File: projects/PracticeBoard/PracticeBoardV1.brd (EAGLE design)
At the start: 160 x 100 mm, 31 parts, among them U1 TPS63001, U3 SNX4AHC08-QUAD-2IN-AND, U4 SN74LV32A-QUAD-2IN-OR

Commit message: PracticeBoardV1 Schematic Review
Added led enable circuit and nonfunctional components
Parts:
- removed R7: (no value), BrownSpaceEngineering:0805
- added C26: 1uF, BrownSpaceEngineering:0805
- added C27, C28: 0.01uF, BrownSpaceEngineering:0805
- added D6: 1N4148SOD-523F, BrownSpaceEngineering:SOD-523F
- added D7: LED0805, BrownSpaceEngineering:0805-D
- added R23: 91K, BrownSpaceEngineering:0805
- added R24, R25: 10K, BrownSpaceEngineering:0805
- added R6: (no value), BrownSpaceEngineering:0805
- added U5: (no value), BrownSpaceEngineering:SO-8
- added U6: SN74LV00A-QUAD-2IN-NAND, BrownSpaceEngineering:TSSOP-14
- added U7: (no value), BrownSpaceEngineering:TSSOP-14
- added U8: SNX4LV86A-QUAD-2IN-XOR, BrownSpaceEngineering:TSSOP-14
- added U9: UA741-OP-AMP, BrownSpaceEngineering:SOIC-8
- added V8: IN4, BrownSpaceEngineering:VIA-60MIL-SQ
- added V9: OUT4, BrownSpaceEngineering:VIA-60MIL-SQ
- R5: device BrownSpaceEngineering:1210 -> BrownSpaceEngineering:0805
- moved R5 241.4 mm to (-4.00, -32.0)
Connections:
- new net !LED_CMD!: C28.1, R25.2, R6.2, V9.P$1
- new net LED_SHDN: D7.A, U5.P$3
- new net N$20: C26.1, R23.2, U5.P$6, U5.P$7
- new net N$23: C27.1, U5.P$5
- new net TRIG: C28.2, D6.A, R24.2, U5.P$2
- net +3V3: now also D6.C, R23.1, R24.1, R25.1, R5.2, U5.P$4, U5.P$8, V8.P$1; no longer R7.2
- net GND: now also C26.2, C27.2, D7.C, R6.1, U5.P$1
- net N$7: now also R5.1; no longer R7.1
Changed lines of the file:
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@@
 <?xml version="1.0" encoding="utf-8"?>
 <!DOCTYPE eagle SYSTEM "eagle.dtd">
-<eagle version="8.3.1">
+<eagle version="8.2.2">
 <drawing>
 <settings>
@@
 <element name="BATTERY" library="BrownSpaceEngineering" package="BC-2003-COIN-BATTERY-HOLDER" value="BC-2003-COIN-BATTERY-HOLDER" x="14" y="-10"/>
 <element name="U2" library="BrownSpaceEngineering" package="SO-8" value="" x="-3" y="-13"/>
-<element name="R7" library="BrownSpaceEngineering" package="0805" value="" x="-4" y="-32"/>
+<element name="R5" library="BrownSpaceEngineering" package="0805" value="" x="-4" y="-32"/>
 <element name="C4" library="BrownSpaceEngineering" package="0805" value="0.01uF" x="-4" y="-42"/>
 <element name="C5" library="BrownSpaceEngineering" package="0805" value="" x="-4" y="-47"/>
@@
 <element name="D4" library="BrownSpaceEngineering" package="0805-D" value="LED0805" x="-12" y="-271"/>
 <element name="D5" library="BrownSpaceEngineering" package="0805-D" value="LED0805" x="-12" y="-276"/>
-<element name="R5" library="BrownSpaceEngineering" package="1210" value="" x="-18" y="-273"/>
+<element name="U5" library="BrownSpaceEngineering" package="SO-8" value="" x="-10" y="-284"/>
+<element name="C26" library="BrownSpaceEngineering" package="0805" value="1uF" x="-12" y="-292"/>
+<element name="C27" library="BrownSpaceEngineering" package="0805" value="0.01uF" x="-8" y="-292"/>
+<element name="C28" library="BrownSpaceEngineering" package="0805" value="0.01uF" x="-4" y="-292"/>
+<element name="R23" library="BrownSpaceEngineering" package="0805" value="91K" x="-12" y="-296"/>
+<element name="R24" library="BrownSpaceEngineering" package="0805" value="10K" x="-8" y="-296"/>
+<element name="R25" library="BrownSpaceEngineering" package="0805" value="10K" x="-4" y="-296"/>
+<element name="D6" library="BrownSpaceEngineering" package="SOD-523F" value="1N4148SOD-523F" x="-5" y="-281"/>
+<element name="V8" library="BrownSpaceEngineering" package="VIA-60MIL-SQ" value="IN4" x="-3" y="-310"/>
+<element name="V9" library="BrownSpaceEngineering" package="VIA-60MIL-SQ" value="OUT4" x="-3" y="-333"/>
+<element name="R6" library="BrownSpaceEngineering" package="0805" value="" x="-12" y="-347"/>
+<element name="D7" library="BrownSpaceEngineering" package="0805-D" value="LED0805" x="-12" y="-352"/>
+<element name="U6" library="BrownSpaceEngineering" package="TSSOP-14" value="SN74LV00A-QUAD-2IN-NAND" x="-18" y="-349"/>
+<element name="U7" library="BrownSpaceEngineering" package="TSSOP-14" value="" x="-26" y="-349"/>
+<element name="U8" library="BrownSpaceEngineering" package="TSSOP-14" value="SNX4LV86A-QUAD-2IN-XOR" x="-34" y="-349"/>
+<element name="U9" library="BrownSpaceEngineering" package="SOIC-8" value="UA741-OP-AMP" x="-41" y="-348"/>
 </elements>
 <signals>
@@
 <vertex x="160" y="0"/>
 </polygon>
-<contactref element="R7" pad="2"/>
+<contactref element="R5" pad="2"/>
 <contactref element="U2" pad="P$8"/>
 <contactref element="U2" pad="P$4"/>
@@
 <contactref element="U3" pad="P14"/>
 <contactref element="U4" pad="P14"/>
+<contactref element="U5" pad="P$8"/>
+<contactref element="U5" pad="P$4"/>
+<contactref element="R24" pad="1"/>
+<contactref element="R25" pad="1"/>
+<contactref element="D6" pad="C"/>
+<contactref element="V8" pad="P$1"/>
+<contactref element="R23" pad="1"/>
 <wire x1="-3" y1="-188" x2="-3" y2="-234" width="0" layer="19" extent="1-1"/>
 <wire x1="-3" y1="-142" x2="-3" y2="-188" width="0" layer="19" extent="1-1"/>
 <wire x1="-4.725" y1="-127.75" x2="-3" y2="-142" width="0" layer="19" extent="1-1"/>
 <wire x1="-11.95" y1="-122.2" x2="-4.725" y2="-127.75" width="0" layer="19" extent="1-1"/>
+<wire x1="-5" y1="-280" x2="-3" y2="-234" width="0" layer="19" extent="1-1"/>
+<wire x1="-11.905" y1="-281.1" x2="-5" y2="-280" width="0" layer="19" extent="1-1"/>
+<wire x1="-8.095" y1="-286.9" x2="-11.905" y2="-281.1" width="0" layer="19" extent="1-1"/>
+<wire x1="-8.9" y1="-296" x2="-8.095" y2="-286.9" width="0" layer="19" extent="1-1"/>
+<wire x1="-12.9" y1="-296" x2="-8.9" y2="-296" width="0" layer="19" extent="1-1"/>
+<wire x1="-4.9" y1="-296" x2="-8.9" y2="-296" width="0" layer="19" extent="1-1"/>
+<wire x1="-3" y1="-310" x2="-4.9" y2="-296" width="0" layer="19" extent="1-1"/>
 <wire x1="-3.1" y1="-32" x2="-11.95" y2="-122.2" width="0" layer="19" extent="1-1"/>
 <wire x1="-1.095" y1="-15.9" x2="-3.1" y2="-32" width="0" layer="19" extent="1-1"/>
@@
 <contactref element="D4" pad="C"/>
 <contactref element="U3" pad="P7"/>
+<contactref element="U5" pad="P$1"/>
+<contactref element="C26" pad="2"/>
+<contactref element="C27" pad="2"/>
+<contactref element="R6" pad="1"/>
+<contactref element="D7" pad="C"/>
 <wire x1="102.49" y1="51.6" x2="106.3" y2="51.6" width="0" layer="19" extent="1-1"/>
 <wire x1="95.21" y1="51.6" x2="102.49" y2="51.6" width="0" layer="19" extent="1-1"/>
@@
 <wire x1="-11.1" y1="-271" x2="-8.05" y2="-127.8" width="0" layer="19" extent="1-1"/>
 <wire x1="-11.1" y1="-276" x2="-11.1" y2="-271" width="0" layer="19" extent="1-1"/>
+<wire x1="-11.905" y1="-286.9" x2="-11.1" y2="-276" width="0" layer="19" extent="1-1"/>
+<wire x1="-11.1" y1="-292" x2="-11.905" y2="-286.9" width="0" layer="19" extent="1-1"/>
+<wire x1="-7.1" y1="-292" x2="-11.1" y2="-292" width="0" layer="19" extent="1-1"/>
+<wire x1="-12.9" y1="-347" x2="-11.1" y2="-292" width="0" layer="19" extent="1-1"/>
+<wire x1="-11.1" y1="-352" x2="-12.9" y2="-347" width="0" layer="19" extent="1-1"/>
 </signal>
 <signal name="3V3REF">
@@
 </signal>
 <signal name="N$7">
-<contactref element="R7" pad="1"/>
+<contactref element="R5" pad="1"/>
 <contactref element="U2" pad="P$7"/>
 <contactref element="POTENTIOMETER-OUT" pad="P$1"/>
@@
 <wire x1="-12.9" y1="-276" x2="-8.7" y2="-127.8" width="0" layer="19" extent="1-1"/>
 </signal>
+<signal name="N$20">
+<contactref element="R23" pad="2"/>
+<contactref element="U5" pad="P$7"/>
+<contactref element="U5" pad="P$6"/>
+<contactref element="C26" pad="1"/>
+<wire x1="-12.9" y1="-292" x2="-11.1" y2="-296" width="0" layer="19" extent="1-1"/>
+<wire x1="-10.635" y1="-281.1" x2="-12.9" y2="-292" width="0" layer="19" extent="1-1"/>
+<wire x1="-9.365" y1="-281.1" x2="-10.635" y2="-281.1" width="0" layer="19" extent="1-1"/>
+</signal>
+<signal name="N$23">
+<contactref element="C27" pad="1"/>
+<contactref element="U5" pad="P$5"/>
+<wire x1="-8.095" y1="-281.1" x2="-8.9" y2="-292" width="0" layer="19" extent="1-1"/>
+</signal>
+<signal name="TRIG">
+<contactref element="C28" pad="2"/>
+<contactref element="U5" pad="P$2"/>
+<contactref element="R24" pad="2"/>
+<contactref element="D6" pad="A"/>
+<wire x1="-3.1" y1="-292" x2="-7.1" y2="-296" width="0" layer="19" extent="1-1"/>
+<wire x1="-10.635" y1="-286.9" x2="-3.1" y2="-292" width="0" layer="19" extent="1-1"/>
+<wire x1="-5" y1="-282" x2="-10.635" y2="-286.9" width="0" layer="19" extent="1-1"/>
+</signal>
+<signal name="!LED_CMD!">
+<contactref element="R25" pad="2"/>
+<contactref element="C28" pad="1"/>
+<contactref element="V9" pad="P$1"/>
+<contactref element="R6" pad="2"/>
+<wire x1="-3" y1="-333" x2="-11.1" y2="-347" width="0" layer="19" extent="1-1"/>
+<wire x1="-3.1" y1="-296" x2="-3" y2="-333" width="0" layer="19" extent="1-1"/>
+<wire x1="-4.9" y1="-292" x2="-3.1" y2="-296" width="0" layer="19" extent="1-1"/>
+</signal>
+<signal name="LED_SHDN">
+<contactref element="U5" pad="P$3"/>
+<contactref element="D7" pad="A"/>
+<wire x1="-9.365" y1="-286.9" x2="-12.9" y2="-352" width="0" layer="19" extent="1-1"/>
+</signal>
 </signals>

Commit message: PracticeBoardV1 Schematic Review II
> Added thru-hole diode and potentiometer to library
> Added via "switch" to the battery
> Added a second battery in series (each one has end-to-end voltage of
~2V)
> Removed unnecessary components
> Fixed (?) astable timing circuit
> Added 150R resistors in series with each LED
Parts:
- removed POTENTIOMETER-IN, POTENTIOMETER-OUT: (no value), BrownSpaceEngineering:VIA-60MIL-SQ
- removed U6: SN74LV00A-QUAD-2IN-NAND, BrownSpaceEngineering:TSSOP-14
- removed U7: (no value), BrownSpaceEngineering:TSSOP-14
- removed U8: SNX4LV86A-QUAD-2IN-XOR, BrownSpaceEngineering:TSSOP-14
- removed U9: UA741-OP-AMP, BrownSpaceEngineering:SOIC-8
- added B1: BC-2003-COIN-BATTERY-HOLDER, BrownSpaceEngineering:BC-2003-COIN-BATTERY-HOLDER
- added D8: 1N914BTR-DIODE, BrownSpaceEngineering:1N914BTR
- added R7, R8, R9: 150R, BrownSpaceEngineering:0805
- added V10: IN5, BrownSpaceEngineering:VIA-60MIL-SQ
- added V11: OUT5, BrownSpaceEngineering:VIA-60MIL-SQ
- C4: value 0.01uF -> 1nF
- C5: value (none) -> 0.1mF
- D1: value MSP3V3 -> 1N914BTR-DIODE; device BrownSpaceEngineering:MICROSMP -> BrownSpaceEngineering:1N914BTR
- R3: value 10K -> 20K; device BrownSpaceEngineering:0805 -> BrownSpaceEngineering:P160KN
- R5: value (none) -> 10K
- R6: value (none) -> 150R
- moved D1 543.0 mm to (-32.0, -476.0)
- moved R3 519.3 mm to (-30.0, -460.0)
- moved R4 475.4 mm to (-43.0, -410.0)
- moved R6 92.4 mm to (-43.0, -434.0)
- renumbered BATTERY to B2
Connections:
- removed net 3V3REF: R3.2, R4.2
- new net N$15: B2.+(1), B2.+(2), V10.P$1
- new net N$16: D8.A, R3.P3, U2.P$7
- new net N$17: R3.P1, R4.2
- new net N$18: B1.+(1), B1.+(2), B2.-
- new net N$19: D7.C, R6.1
- new net N$21: D5.C, R7.2
- new net N$22: D3.C, R9.2
- new net N$24: D4.C, R8.1
- new net N$25: D1.C, R4.1
- net !LED_CMD!: no longer R6.2
- net +3V3: no longer D1.C, R3.1, V8.P$1
- net GND: now also B1.-, R6.2, R7.1, R8.2, R9.1, V8.P$1; no longer B2.-, D1.A, D3.C, D4.C, D5.C, D7.C, R4.1, R6.1
- net N$3: now also D1.A, D8.C; no longer POTENTIOMETER-IN.P$1
- net N$7: now also R3.P2; no longer POTENTIOMETER-OUT.P$1, U2.P$7
- net VIN: now also V11.P$1; no longer B2.+(1), B2.+(2)

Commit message: PracticeBoardV1 Board Review
Library
> Removed the quad 2in AND gate symbol and replaced with the other
generic quad 2in gate symbol
> Consolidated quad 2in gates into one symbol and device with multiple
package variants
> Changed diode to part 1N4148; added it's thru-hole package as a
package variant to the existing 1N4148 device (and changed the existing
package's name to SMD)
ControlBoardV3
> Updated the 1N4148 diode to reflect the change in the package
variant's name
PracticeBoardV1
> Minor changes to schematic
> Board layout started and finished
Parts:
- removed B2: BC-2003-COIN-BATTERY-HOLDER, BrownSpaceEngineering:BC-2003-COIN-BATTERY-HOLDER
- added V12: LED_SHDN, BrownSpaceEngineering:VIA-60MIL-SQ
- added V13: ASTABLE_OUT, BrownSpaceEngineering:VIA-60MIL-SQ
- B1: value BC-2003-COIN-BATTERY-HOLDER -> Use BR2032 - 3V (2V END POINT)
- D1, D8: value 1N914BTR-DIODE -> 1N4148THRU-HOLE; device BrownSpaceEngineering:1N914BTR -> BrownSpaceEngineering:1N4148
- D6: value 1N4148SOD-523F -> 1N4148SOD-523FSMD
- U3: value SNX4AHC08-QUAD-2IN-AND -> AND
- U4: value SN74LV32A-QUAD-2IN-OR -> OR
- moved D8 519.2 mm to (48.0, 23.0), turned to 90 degrees
- moved D1 508.8 mm to (38.0, 28.0), turned to 270 degrees
- moved R6 495.8 mm to (26.0, 57.0)
- moved R7 494.2 mm to (35.0, 49.0), turned to 180 degrees
- moved R8 492.9 mm to (50.0, 40.0), turned to 90 degrees
- moved R3 471.7 mm to (43.0, 6.00)
- moved R9 468.9 mm to (53.0, 10.0), turned to 270 degrees
- moved B1 439.9 mm to (10.0, 16.0), turned to 270 degrees
- moved R4 433.6 mm to (38.0, 16.0), turned to 270 degrees
- moved V11 425.1 mm to (18.0, 33.0), turned to 180 degrees
- moved D7 410.4 mm to (22.0, 57.0)
- moved V10 401.6 mm to (13.0, 33.0), turned to 180 degrees
- moved V9 377.4 mm to (15.0, 44.0)
- moved V8 359.5 mm to (15.0, 49.0)
- moved C27 351.3 mm to (7.00, 59.0), turned to 180 degrees
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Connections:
- removed net N$15: B2.+(1), B2.+(2), V10.P$1
- removed net N$18: B1.+(1), B1.+(2), B2.-
- new net ASTABLE_OUT: D3.A, U2.P$3, V13.P$1
- net GND: now also U3.P10, U3.P12, U3.P13, U3.P9, U4.P10, U4.P12, U4.P13, U4.P9
- net LED_SHDN: now also V12.P$1
- net N$1: now also B1.+(1), B1.+(2), V10.P$1; no longer D3.A, U2.P$3
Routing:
- net DIM-WIRE: track 520.0 -> 260.0 mm
- net GND: track 0.00 -> 85.1 mm, vias 0 -> 10
- net N$12: track 0.00 -> 37.5 mm
- net N$1: track 0.00 -> 34.6 mm
- net N$3: track 0.00 -> 31.9 mm
- net N$11: track 0.00 -> 29.8 mm
- net N$16: track 0.00 -> 19.3 mm
- net N$10: track 0.00 -> 17.1 mm
- net VIN: track 0.00 -> 11.7 mm
- net !LED_CMD!: track 0.00 -> 9.48 mm
- net N$7: track 0.00 -> 9.10 mm
- net N$17: track 0.00 -> 9.10 mm
- net LED_SHDN: track 0.00 -> 8.81 mm
- net ASTABLE_OUT: track 0.00 -> 8.81 mm
- net TRIG: track 0.00 -> 8.32 mm
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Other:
- board size 160 x 100 mm -> 65 x 65 mm
- board text added: "BSE August 2017 EQUiSat Practice Board V1"
- board text added: "Use BR2032 Coin Battery"

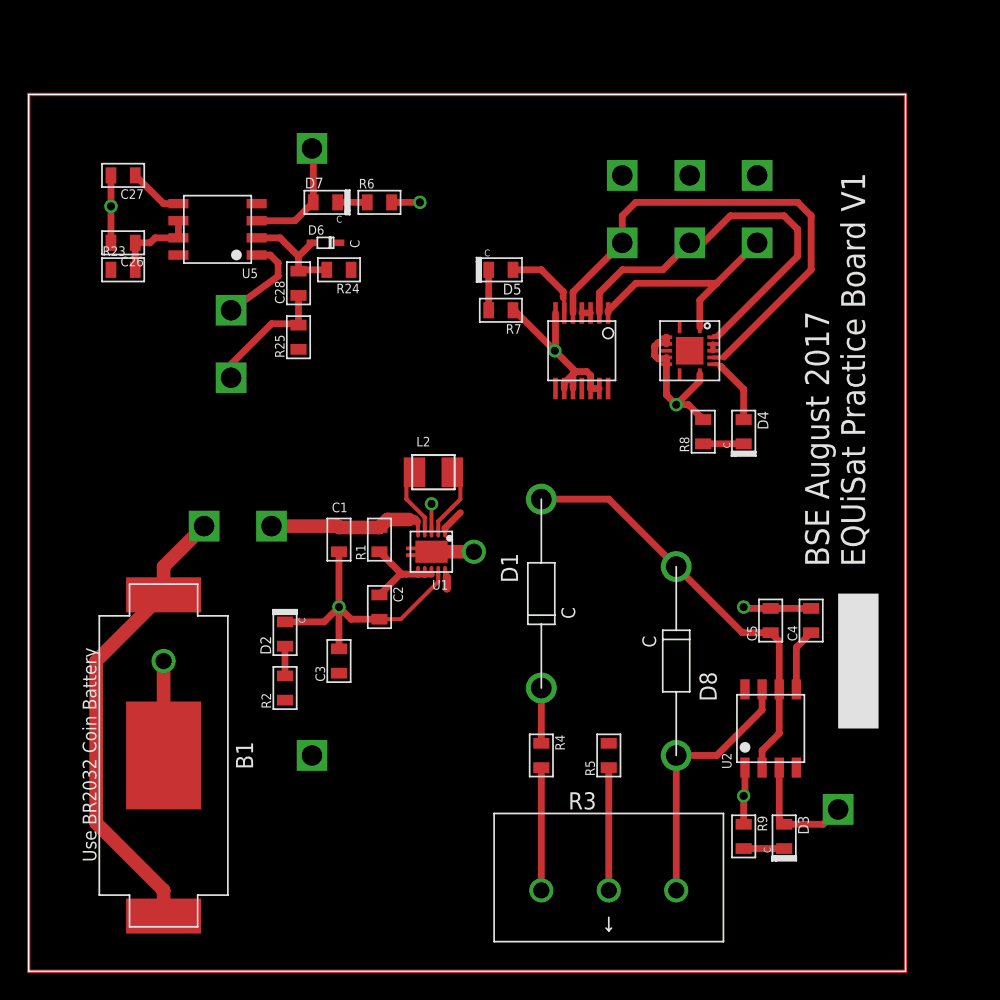
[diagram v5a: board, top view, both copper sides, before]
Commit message: Adjusted board layout for sizing. Added notes to silkscreen for ease of operation. Removed bottom silkscreen. Added 10k pull-down resistors to logic inputs.
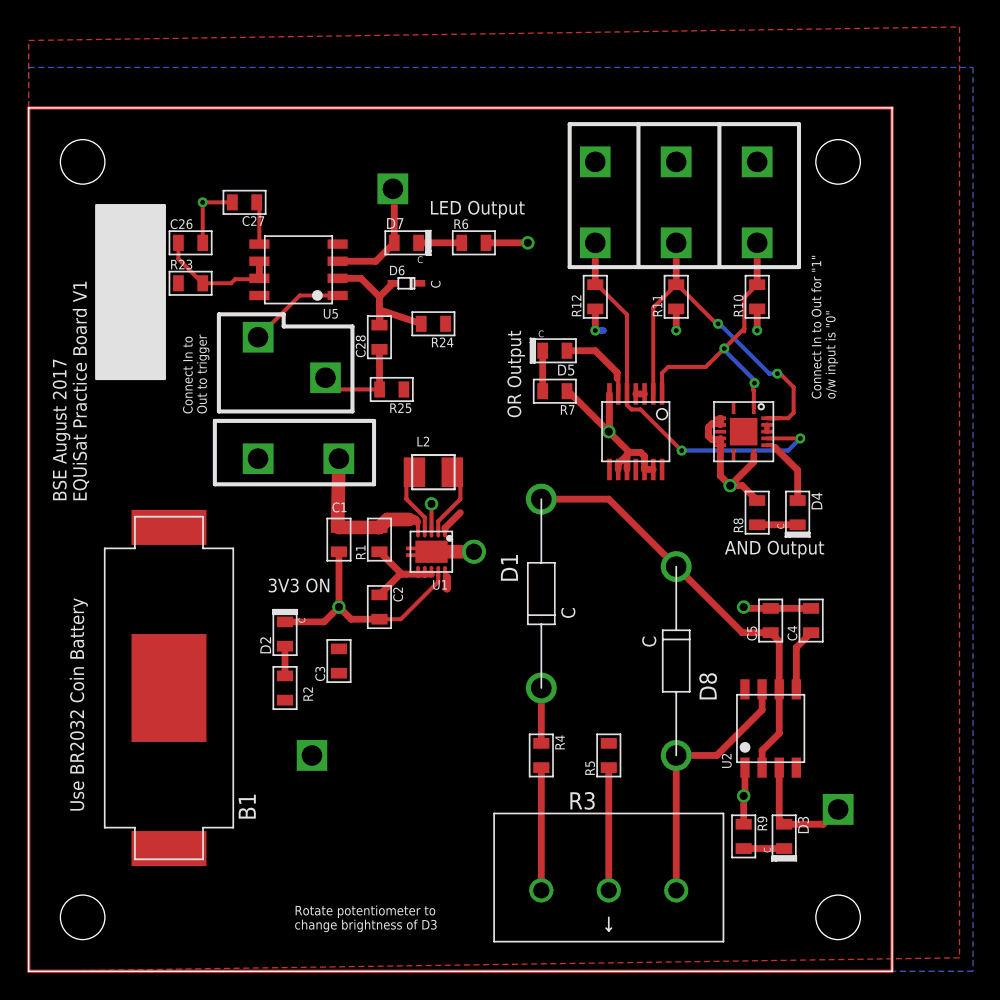
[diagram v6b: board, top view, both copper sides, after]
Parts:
- added R10, R11, R12: 10K, BrownSpaceEngineering:0805
- V10: value IN5 -> BATT
- V11: value OUT5 -> INPUT
- moved C27 9.22 mm to (16.0, 57.0)
- moved R24 8.06 mm to (30.0, 48.0)
- moved R25 7.92 mm to (26.9, 43.1), turned to 180 degrees
- moved R6 7.62 mm to (33.0, 54.0)
- moved C28 7.21 mm to (26.0, 47.0)
- moved D4 7.21 mm to (57.0, 34.0)
- moved D5 7.21 mm to (39.0, 46.0)
- moved R7 7.21 mm to (39.0, 43.0)
- moved R8 7.21 mm to (54.0, 34.0)
- moved U3 7.21 mm to (53.0, 40.0)
- moved U4 7.21 mm to (45.0, 40.0)
- moved V11 7.07 mm to (23.0, 38.0), turned to 0 degrees
- moved V9 7.00 mm to (22.0, 44.0)
- moved D6 6.71 mm to (28.0, 51.0)
- moved D7 6.71 mm to (28.0, 54.0)
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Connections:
- net GND: now also R10.1, R11.1, R12.1
- net N$10: now also R10.2
- net N$11: now also R11.2
- net N$12: now also R12.2
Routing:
- net N$1: track 34.6 -> 0.00 mm
- net N$12: track 37.5 -> 30.2 mm, vias 0 -> 2
- net N$10: track 17.1 -> 21.6 mm, vias 0 -> 2
- net DIM-WIRE: track 260.0 -> 256.0 mm
- net GND: track 85.1 -> 81.8 mm, vias 10 -> 12
- net TRIG: track 8.32 -> 11.4 mm
- net N$20: track 6.62 -> 9.37 mm
- net !LED_CMD!: track 9.48 -> 7.34 mm
- net N$19: track 2.20 -> 3.20 mm
- net N$11: track 29.8 -> 28.8 mm, vias 0 -> 2
- net N$23: track 4.07 -> 3.18 mm
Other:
- board size 65 x 65 mm -> 64 x 64 mm
- board text added: "3V3 ON"
- board text added: "AND Output"
- board text added: "Connect In to Out for "1" o/w input is "0""
- board text added: "Connect In to Out to trigger"
- board text added: "LED Output"
- board text added: "OR Output"
- board text added: "Rotate potentiometer to change brightness of D3"
